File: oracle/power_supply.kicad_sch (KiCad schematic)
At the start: 12 parts, among them J8 BAT, Q1 AO3407A, Q2 SS8050, U6 CHG_MOD

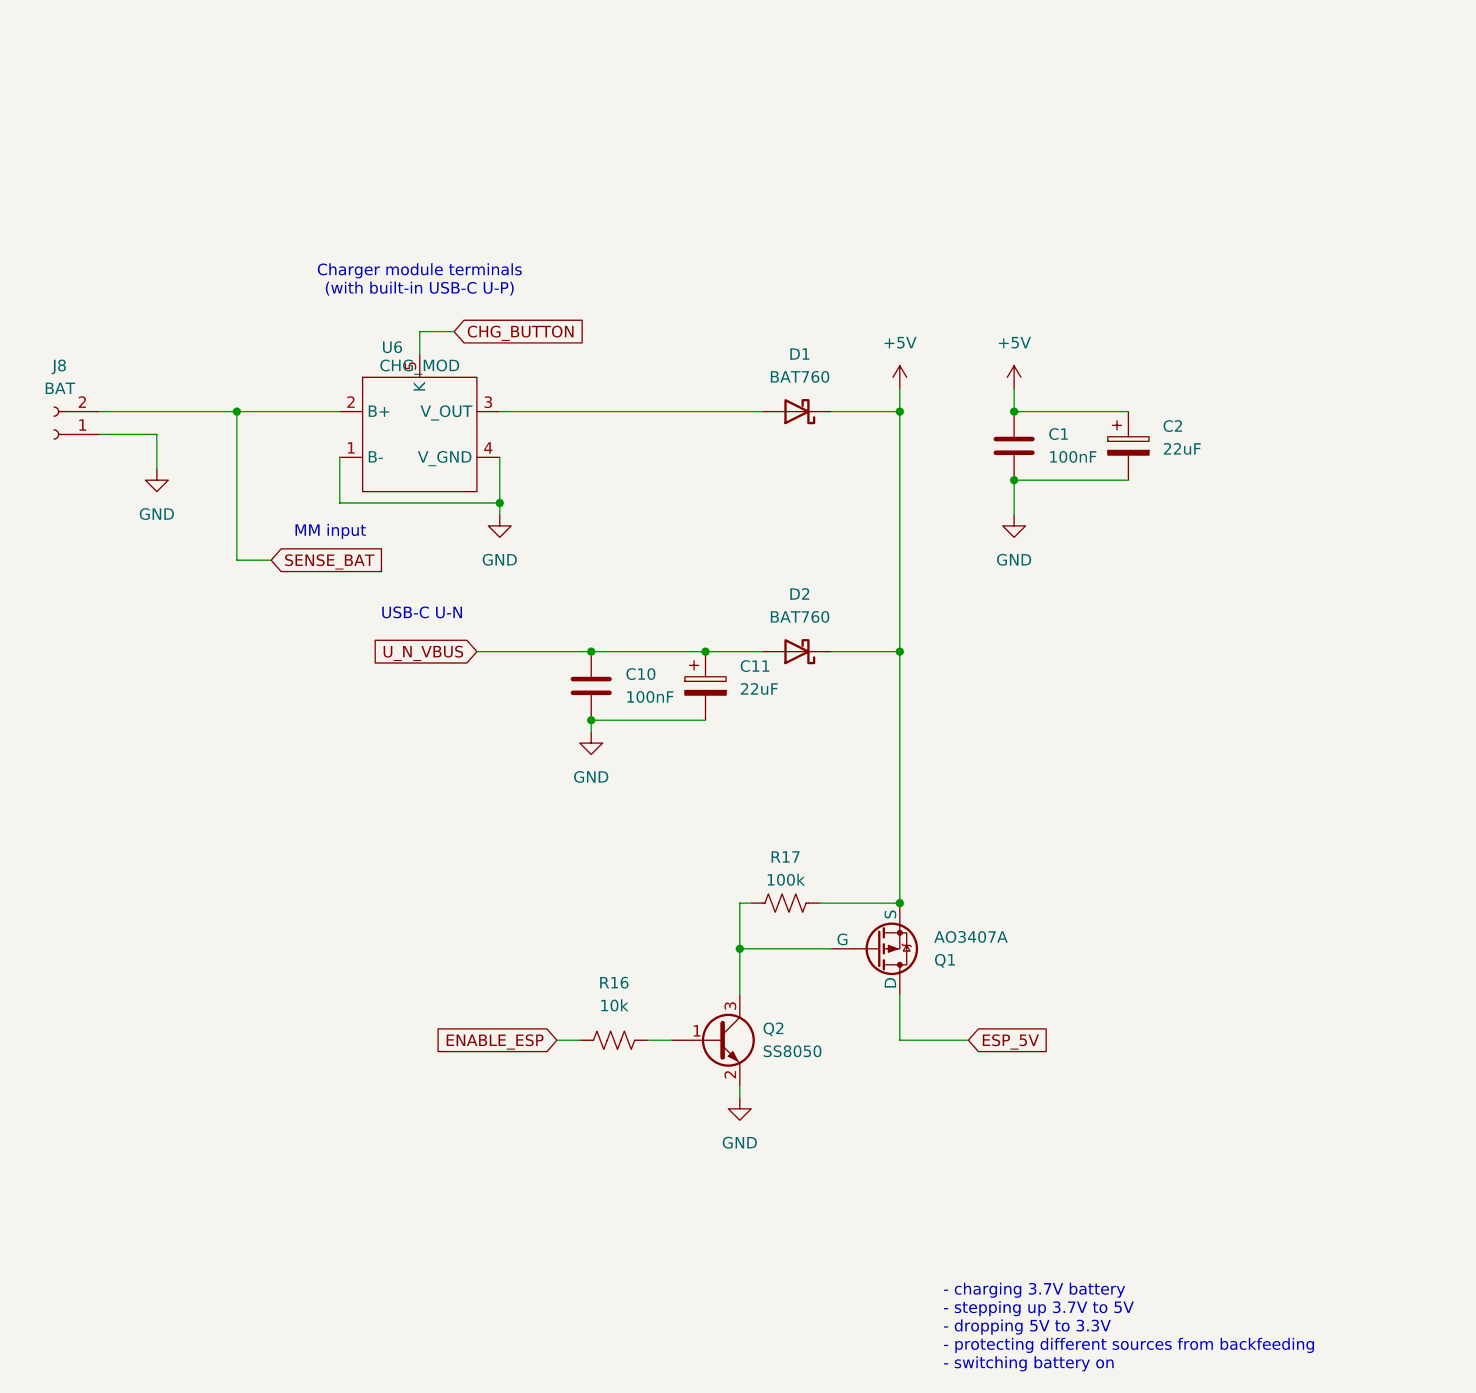
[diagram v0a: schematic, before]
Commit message: add n_core firmware add e_core firmware stub update PCB
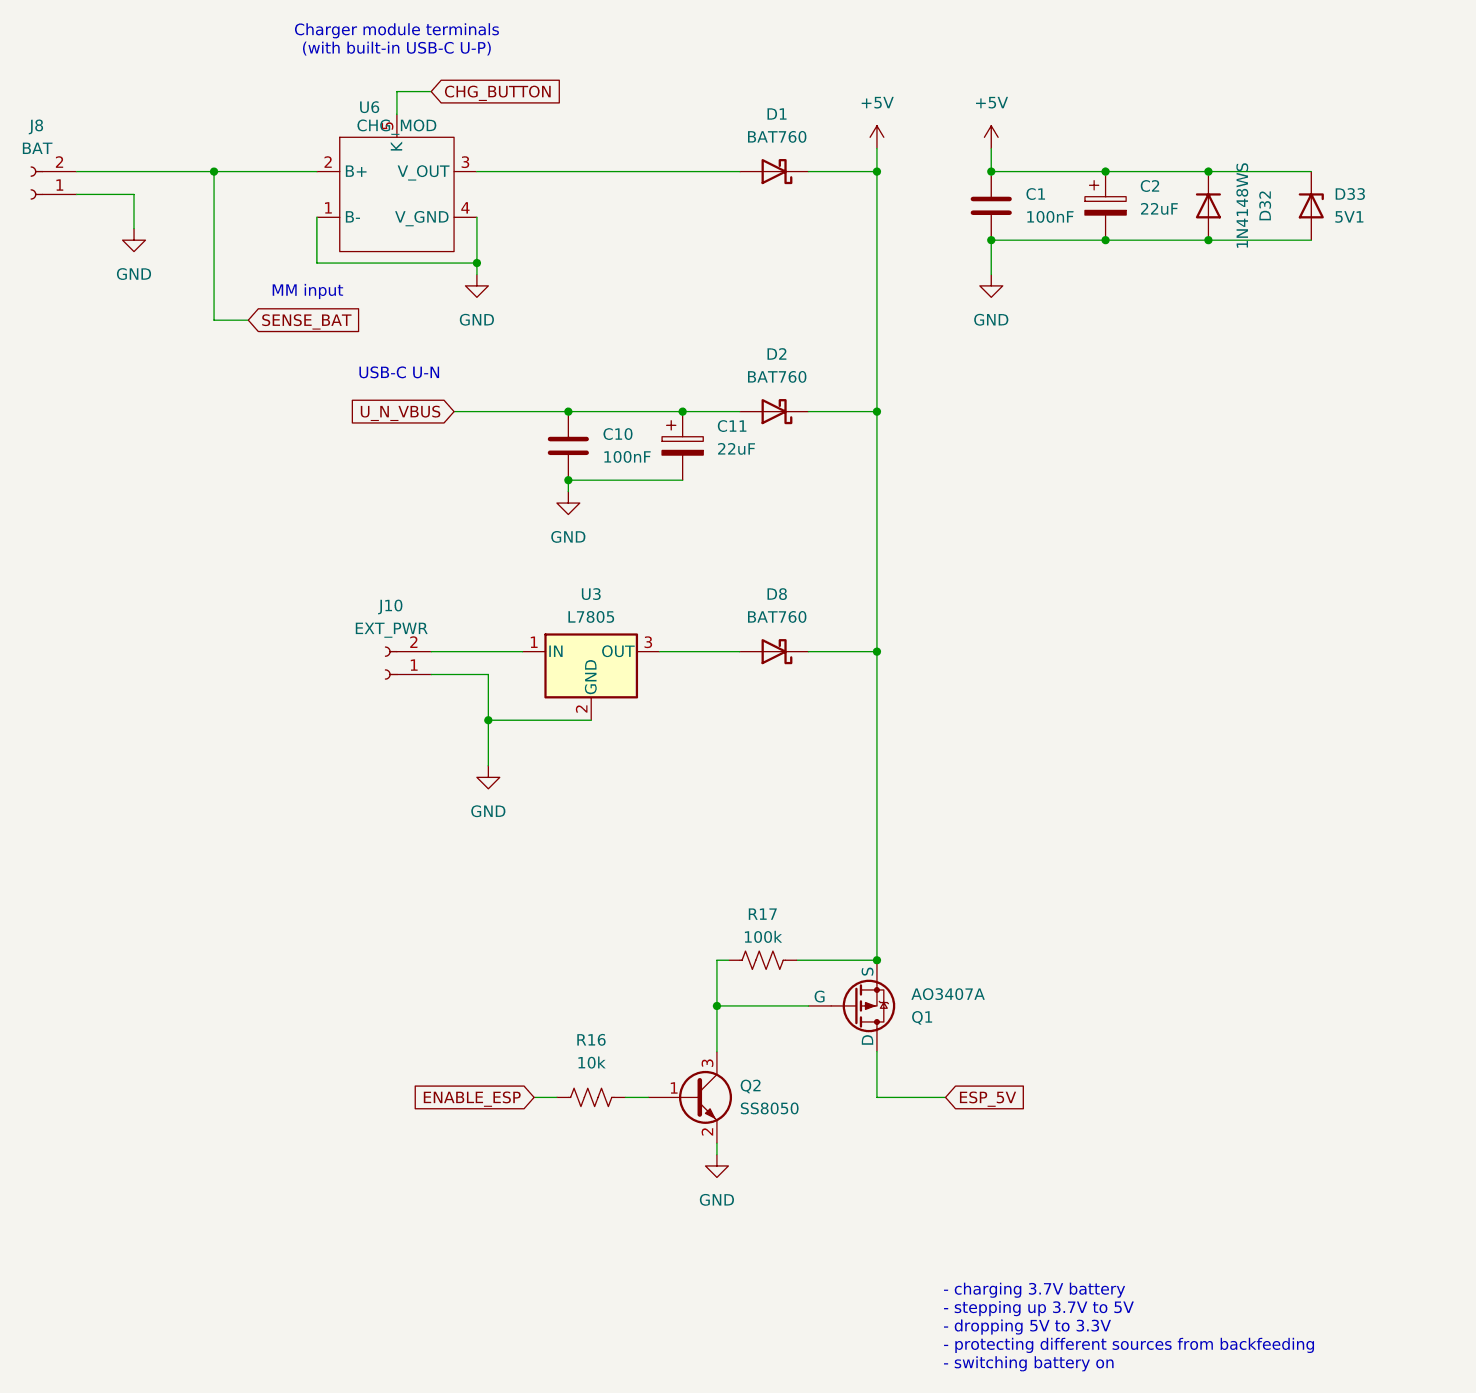
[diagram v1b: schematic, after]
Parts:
- added D32: 1N4148WS, Diode_SMD:D_SOD-323F, symbol Device:D
- added D33: 5V1, Diode_THT:D_DO-15_P10.16mm_Horizontal, symbol Device:D_Zener
- added D8: BAT760, Diode_SMD:D_SOD-323F, symbol Device:D_Schottky
- added J10: EXT_PWR, Connector_PinHeader_2.54mm:PinHeader_2x01_P2.54mm_Vertical, symbol Connector:Conn_01x02_Socket
- added U3: L7805, Package_TO_SOT_SMD:TO-252-2, symbol Regulator_Linear:L7805
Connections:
- net +5V: now also D32.1 (K), D33.1 (K), D8.1 (K)
- net GND: now also D32.2 (A), D33.2 (A), J10.1 (Pin_1), U3.2 (GND)
- new net: J10.2 (Pin_2), U3.1 (IN)
- new net: D8.2 (A), U3.3 (OUT)
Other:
- moved on the sheet: C1, C10, C11, C2, D1, D2, J8, Q1, Q2, R16, R17, U6
